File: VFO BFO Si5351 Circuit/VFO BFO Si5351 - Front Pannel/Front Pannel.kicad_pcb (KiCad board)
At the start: 2 copper layers, 149.4 x 69.2 mm, 23 parts, among them J1 LED, J2 Optical Rotary Encoder, J3 Mecc_rotary encoder, J4 VFO_Front_Pannel, SW1 RotaryEncoder_Clarifier, SW2 SW_Band, SW3 SW_Mode, SW4 SW_AGC, SW5 SW_ATT, SW6 SW_Scan, SW7 SW_Step, SW8 SW_RTTY_CW, U1 Ili9341_Module_TFT_320x240_To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

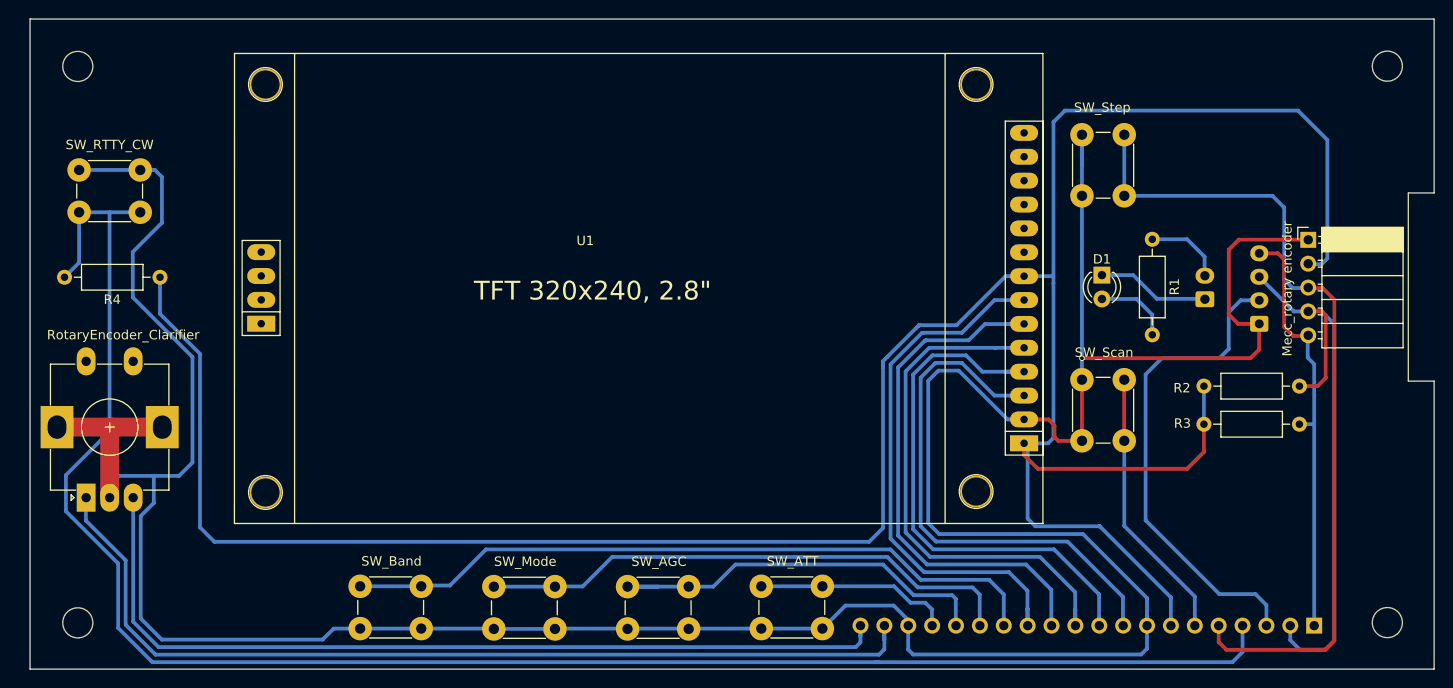
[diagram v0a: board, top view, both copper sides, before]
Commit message: PDF distenta componenti e  schemi elettrico e di montaggio
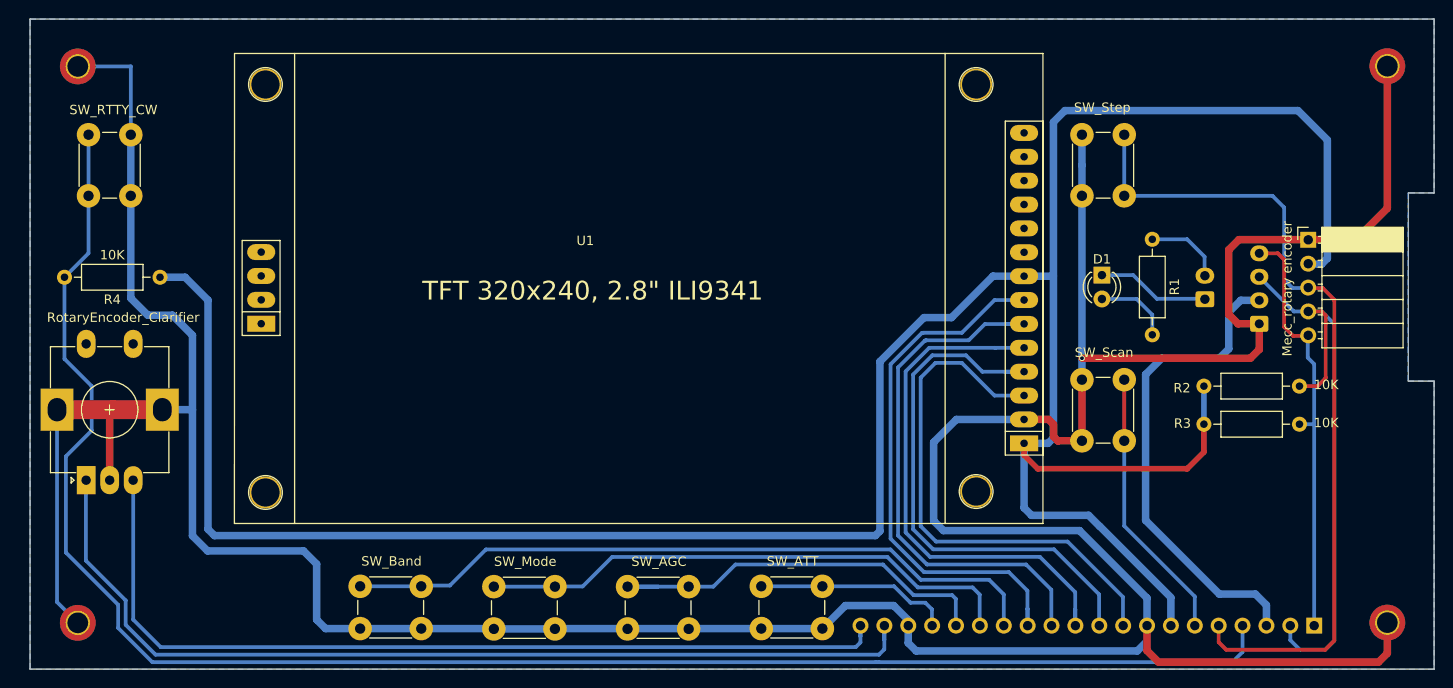
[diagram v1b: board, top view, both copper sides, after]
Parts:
- H1, H2, H3, H4: footprint MountingHole:MountingHole_3.2mm_M3_DIN965 -> MountingHole:MountingHole_2.2mm_M2_DIN965_Pad_TopBottom
- R2, R3: value 4.7K -> 10K
- moved SW8 6.66 mm to (79.1, 69.8), turned to -90 degrees
- moved SW1 1.86 mm to (74.4, 106.6)
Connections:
- D1 pad 1: Net-(D1-K) -> GND
- J1 pad 1: Net-(D1-K) -> GND
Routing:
- net GND: track 351.8 -> 426.5 mm
- net Net-(D1-K): track 12.0 -> 0.00 mm
- net SW_RTTY_CW: track 186.9 -> 182.5 mm
- net CLK-2: track 102.1 -> 104.0 mm
- net DT-2: track 94.6 -> 96.3 mm
- added copper zone on B.Cu, net GND
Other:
- board text added: "ESP32_VFO-BFO_EVO V1.1"
- board text removed: "ESP32_VFO-BFO_EVO V1.0"
